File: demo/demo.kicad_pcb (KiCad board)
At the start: 2 copper layers, 34 x 28 mm, 22 parts, among them J1 USB4105-GF-A, J2 TC2030-NL, U1 STM32F072CBT6, U2 USBLC6-2SC6, U3 TLV1117LV33DCYR

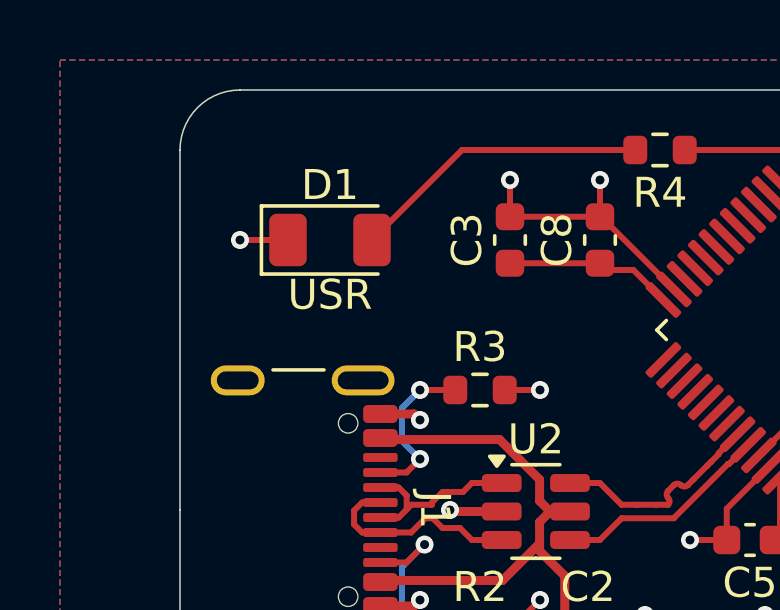
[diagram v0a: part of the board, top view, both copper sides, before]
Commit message: python tool to find kicad files and do erc/drc reports
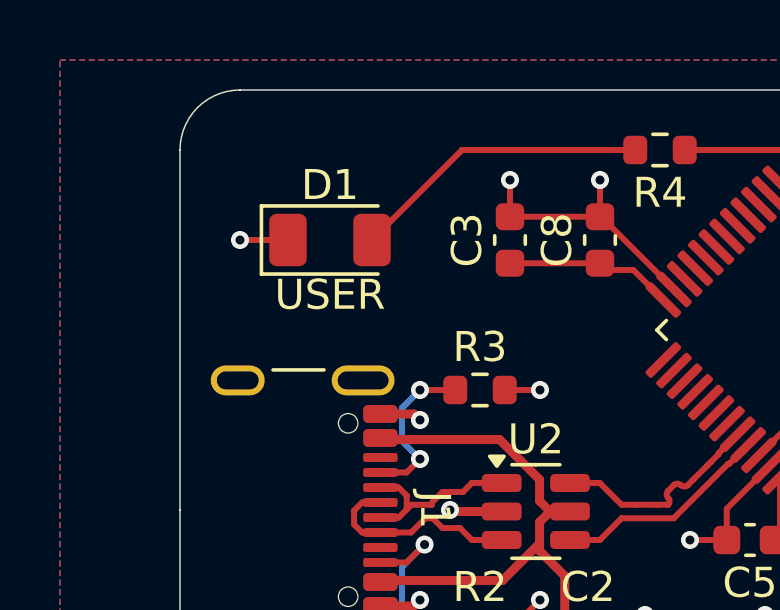
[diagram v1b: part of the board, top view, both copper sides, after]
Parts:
- D1: value USR -> USER
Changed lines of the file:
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@@
 			)
 		)
-		(property "Value" "USR"
+		(property "Value" "USER"
 			(at 0 1.829999 0)
 			(layer "F.SilkS")
